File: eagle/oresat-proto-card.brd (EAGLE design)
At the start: 99.8 x 94.7 mm, 123 parts, among them J1 J-SAMTEC-TFM-110-X1-XXX-D-RA, J2 U.FL, J3 U.FL, J4 U.FL, J6 J-SAMTEC-TFM-120-X1-XXX-D-RA, J7 FTSH-105-XX-X-DV-K, Q1 DMP2240UDM, Q2 DMP2240UDM, Q3 MOSFET-PCH-SOT23-6, Q4 MOSFET-PCH-SOT23-6, Q5 PMV45EN, Q6 PMV45EN, U2 TCAN330, U3 MAX7310ATE, U4 MAX4211CETE, U5 TPS62111RSA, U6 STM32F042K6, X1 16MHZ-2.5x2mm

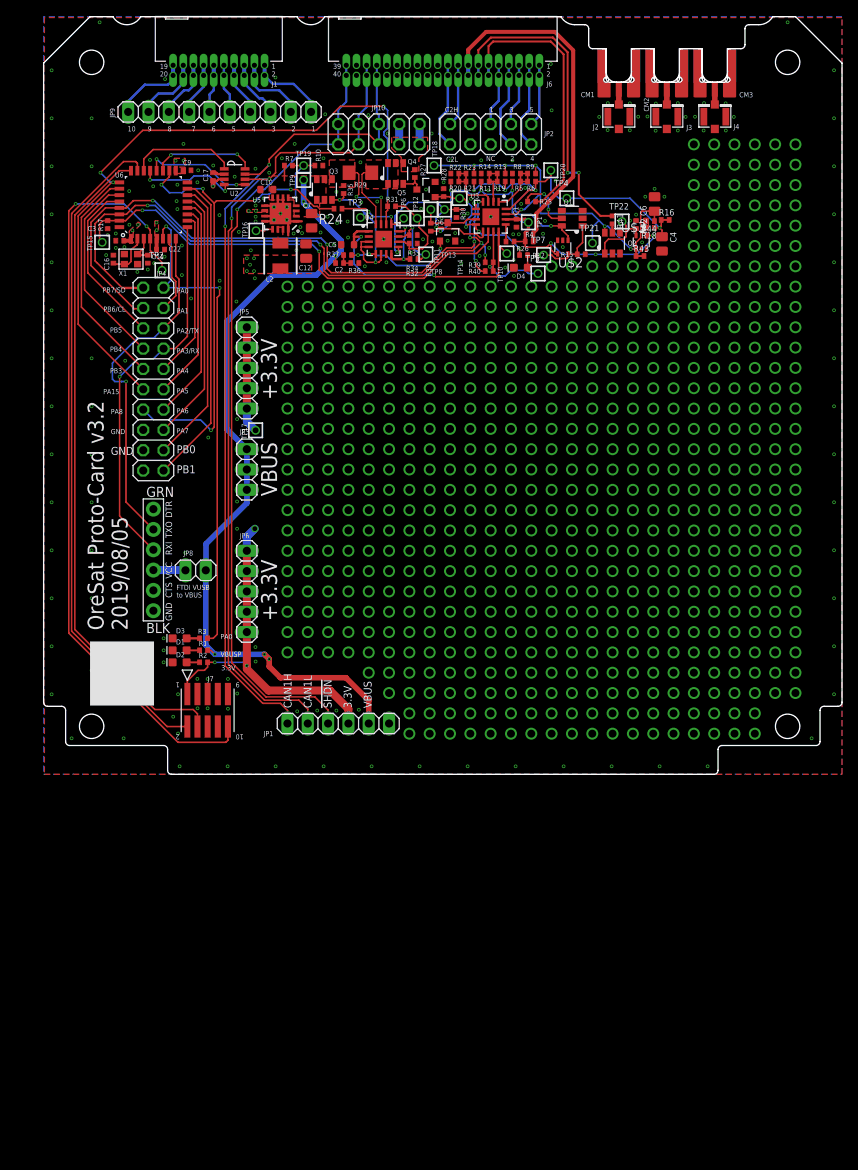
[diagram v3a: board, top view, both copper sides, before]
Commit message: fixed j-tag connect, final tweaks for 3.3, updated bom
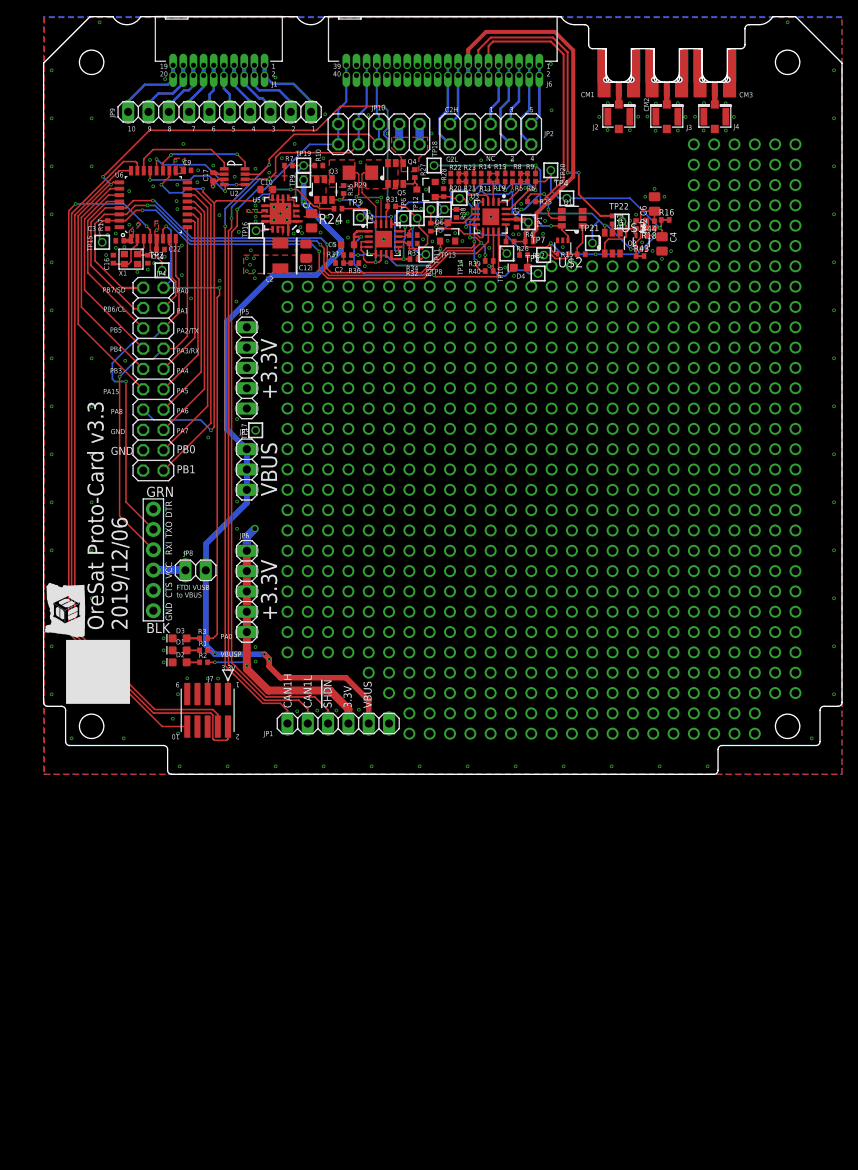
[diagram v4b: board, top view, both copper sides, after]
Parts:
- C4, C6, R16, R18, R43, R44: value NP -> TBD
- R42: value 10k -> TBD
- moved R39 0.17 mm to (55.7, 64.2)
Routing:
- net 3.3V: track 63.1 -> 46.2 mm, vias 17 -> 18
- net SWDIO: track 83.5 -> 92.8 mm
- net NRESET: track 97.7 -> 90.0 mm
- net SWCLK: track 82.4 -> 84.9 mm
- net IOUT: track 88.3 -> 87.5 mm
- net GND: vias 307 -> 306
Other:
- board text added: "2019/12/06"
- board text added: "OreSat Proto-Card v3.3"
- board text removed: "2019/08/05"
- board text removed: "OreSat Proto-Card v3.2"

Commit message: Now v3.3. New OPD I2C protection circuits. Move to 4 layers. Lots of cleanup and massaging, but nothing worth saying. Added ground ring around 3.3V ring on L15. Attributes are still wrong, needs to be cleaned up to make automatic BOM.
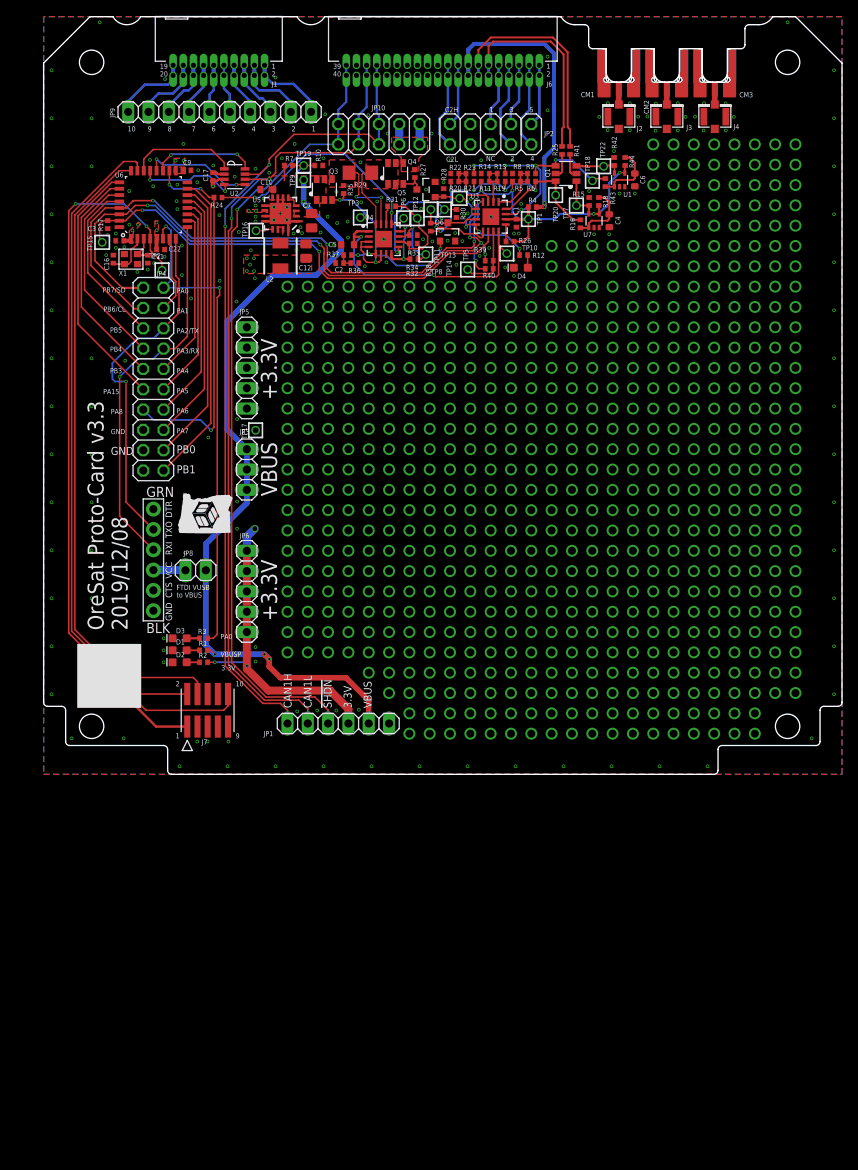
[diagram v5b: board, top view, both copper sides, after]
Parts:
- removed Q2: DMP2240UDM, Q-MOSFET-PCH-dual-SOT23-6:SOT23-6
- removed TP21, TP4: TEST-POINT, Tova:2MM-TEST-POINT
- removed U$2, U$3: MIC842, Q-Microchip-MIC842-Comparator:SC70-5
- added U1, U7: MIC842LYC5, Q-Microchip-MIC842-Comparator:SC70-5
- C4, C6: value TBD -> 1u; device oresat-rcl:.0805-B-NOSILK -> oresat-rcl:.0603-B-NOSILK
- R16, R43: value TBD -> 330k
- R18, R44: value TBD -> 1M
- R42: value TBD -> 10k
- U4: value MAX4211CETE -> MAX4211FETE
- moved TP18 19.9 mm to (68.6, 74.2)
- moved R24 15.1 mm to (21.8, 72.1)
- moved R16 10.6 mm to (67.1, 68.8), turned to 90 degrees
- moved R41 10.2 mm to (65.8, 78.0)
- moved R43 10.1 mm to (70.2, 74.0), turned to 90 degrees
- moved TP5 8.81 mm to (53.0, 63.1)
- moved R42 8.36 mm to (71.3, 76.6)
- moved R44 8.09 mm to (72.7, 76.6), turned to 270 degrees
- moved R25 7.44 mm to (64.8, 78.0), turned to 270 degrees
- moved TP7 7.43 mm to (66.6, 71.1)
- moved TP22 7.27 mm to (70.0, 76.0)
- moved R18 7.23 mm to (69.4, 71.6), turned to 270 degrees
- moved C4 7.21 mm to (70.7, 69.2)
- moved R15 6.68 mm to (68.2, 71.6), turned to 270 degrees
- moved Q1 5.65 mm to (65.3, 75.1)
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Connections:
- new net N$400: C6.1, R43.1, R44.1, U1.1
- new net N$401: C4.1, R16.1, R18.1, U7.1
- new net PA15: JP4.11, U6.25
- net GND: now also U1.2, U7.2; no longer U$2.2, U$3.2
- net IOUT: no longer JP4.11, U6.25
- net N$479: now also Q1.2; no longer Q2.5
- net N$480: now also Q1.3, U1.5; no longer Q2.1, U$3.5
- net N$580: now also U7.5; no longer U$2.5
- net PEN-SCL-FILT: now also Q1.4; no longer C6.1, Q2.6, R43.1, R44.1, TP21.1, U$3.1
- net PEN-SDA-FILT: no longer C4.1, R16.1, R18.1, TP4.1, U$2.1
- net VPD: now also U1.4, U7.4; no longer U$2.4, U$3.4
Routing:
- net IOUT: track 87.5 -> 2.31 mm, vias 4 -> 0
- net PA15: track 0.00 -> 32.0 mm
- net PEN-SDA-FILT: track 54.9 -> 26.2 mm, vias 5 -> 3
- net PEN-SCL-FILT: track 55.0 -> 30.5 mm, vias 6 -> 5
- net POUT: track 9.34 -> 30.6 mm
- net POUTPROT: track 65.2 -> 46.8 mm, vias 5 -> 3
- net OPD_SCL: track 40.2 -> 27.6 mm, vias 2 -> 0
- net SWDIO: track 92.8 -> 81.9 mm
- net OPD_SDA: track 34.3 -> 25.5 mm
- net OPD_PWR: track 44.2 -> 35.9 mm, vias 0 -> 2
- net N$401: track 0.00 -> 8.00 mm
- net N$400: track 0.00 -> 7.86 mm
- net 3.3V: track 46.2 -> 53.8 mm
- net NRESET: track 90.0 -> 95.9 mm
- net N$579: track 7.44 -> 3.08 mm, vias 2 -> 0
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- added copper zone on layer 15, net GND
- removed copper zone on layer 1, net VPD
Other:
- board text added: "2019/12/08"
- board text removed: "2019/12/06"

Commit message: fixing the lock?
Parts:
- J5: value (none) -> DNP

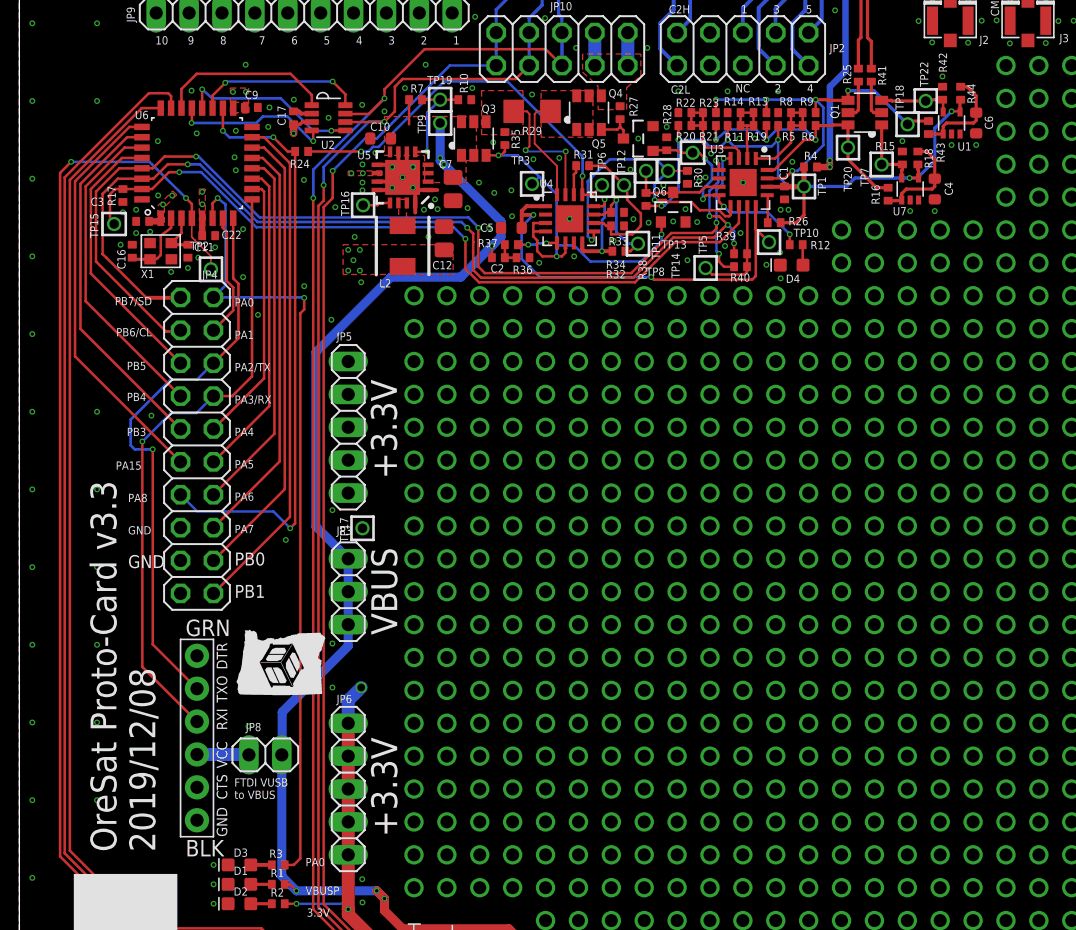
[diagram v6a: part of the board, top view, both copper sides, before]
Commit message: Fixed MIC842L flipped pins. Layout turned out to be better, too!
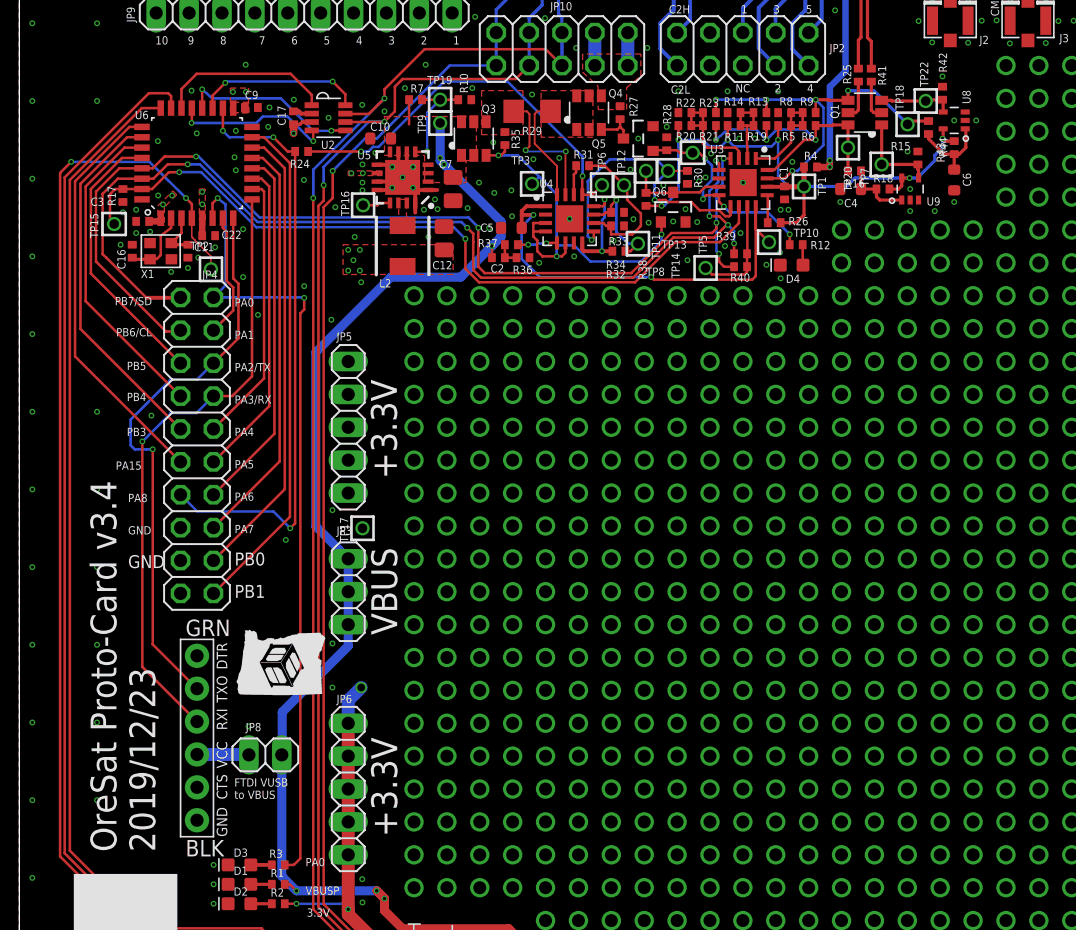
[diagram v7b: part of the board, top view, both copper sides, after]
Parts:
- removed U1, U7: MIC842LYC5, Q-Microchip-MIC842-Comparator:SC70-5
- added U8, U9: MIC842LYC5, U-Microchip-MIC842-Comparator:SC70-5
- moved C4 6.50 mm to (64.2, 69.2), turned to 180 degrees
- moved C6 4.72 mm to (72.2, 69.9)
- moved R44 4.23 mm to (72.2, 72.4), turned to 90 degrees
- moved R18 3.61 mm to (66.7, 69.2), turned to 0 degrees
- moved R16 3.16 mm to (64.5, 70.6), turned to 180 degrees
- moved R15 1.20 mm to (69.4, 71.6)
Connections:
- net GND: now also U8.2, U9.2; no longer U1.2, U7.2
- net N$400: now also U8.1; no longer U1.1
- net N$401: now also U9.1; no longer U7.1
- net N$480: now also U8.4; no longer U1.5
- net N$580: now also U9.4; no longer U7.5
- net VPD: now also U8.5, U9.5; no longer U1.4, U7.4
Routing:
- net PEN-SDA-FILT: track 26.2 -> 23.1 mm
- net N$401: track 8.00 -> 5.25 mm
- net VPD: track 51.7 -> 49.7 mm
- net N$400: track 7.86 -> 6.62 mm
- net N$580: track 5.72 -> 6.92 mm
- net GND: vias 295 -> 298
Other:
- board text added: "2019/12/23"
- board text added: "OreSat Proto-Card v3.4"
- board text removed: "2019/12/08"
- board text removed: "OreSat Proto-Card v3.3"

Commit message: protocard preliminary rev 3.5
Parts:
- removed C11, C16: 20p, rcl_custom:.0402-B-NOSILK
- removed C17, C22, C3, C9: 100n, rcl_custom:.0402-B-NOSILK
- removed D3: AMBER, SparkFun-LED:LED-0603
- removed J5: DNP, SparkFun-Connectors:6_PIN_SERIAL_TARGET_SIDE_W_SILK
- removed JP4: (no value), pinhead:2X10
- removed JP8: (no value), pinhead:1X02
- removed R17: 10k, rcl_custom:.0402-B-NOSILK
- removed R24: 10k, rcl:R0402
- removed R3: 2.7k, rcl_custom:.0402-B-NOSILK
- removed TP15, TP2: TEST-POINT, Tova:2MM-TEST-POINT
- removed U2: TCAN330, TCAN330:SOT23-8_TI-DCN
- removed U6: STM32F042K6, STM32F042K:QFP32-7X7
- removed X1: 16MHZ-2.5x2mm, low-gain-radio:CRYSTAL_2.5X2
- added C13, C14, C19, C20, C21: 100n, oresat-rcl:.0603-C-NOSILK
- added C15, C18: 20p, oresat-rcl:.0603-C-NOSILK
- added D5: AMBER, SparkFun-LED:LED-0603
- added JP7: (no value), pinhead:2X10
- added R47, R49: 10k, oresat-rcl:.0603-C-NOSILK
- added R48, R50, R51: 2.7k, oresat-rcl:.0603-C-NOSILK
- added TP26, TP27, TP28, TP29, TP30, TP31, TP32: TEST-POINT, Tova:2MM-TEST-POINT
- added U1: TCAN330, TCAN330:SOT23-8_TI-DCN
- added U7: STM32F091C, U-ST-STM32F091C-uC:STM32F091C
- added X2: 16MHZ-2.5x2mm, low-gain-radio:CRYSTAL_2.5X2
- J7: value FTSH-105-XX-X-DV-K -> ORESAT-DEBUG-CONNECTOR-CARD; device J-Samtec-FTSH-105-XXX-DV-K-ARM-SWD:CON10_2X5_DUK_FTSH -> oresat-edge_connector:TE_2-1734592-0
- R1, R2: device rcl_custom:.0402-B-NOSILK -> oresat-rcl:.0603-C-NOSILK
- moved JP1 31.2 mm to (18.2, 31.5), turned to 270 degrees
- moved J7 12.2 mm to (32.7, 7.90), turned to 180 degrees
- moved D2 0.30 mm to (17.0, 14.3)
- moved R2 0.30 mm to (20.0, 14.3)
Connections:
- removed net CRYSTALIN: C16.1, U6.2, X1.1
- removed net CRYSTALOUT: C11.1, U6.3, X1.3
- removed net N$1: D3.A, R3.1
- removed net N$406: J5.P$4, JP8.2
- new net CRYSTALIN1: C18.1, U7.5, X2.1
- new net CRYSTALOUT1: C15.1, U7.6, X2.3
- new net N$522: D5.A, R48.1
- new net N$523: J7.20, TP31.1
- new net N$524: J7.19, TP30.1
- new net N$525: J7.18, TP29.1
- new net N$526: J7.17, TP28.1
- new net N$527: J7.16, TP32.1
- new net VBAT: U7.1
- net 3.3V: now also C13.2, C14.2, C19.2, C20.2, C21.2, J7.11, R50.2, R51.2, U1.3, U7.24, U7.36, U7.48, U7.9; no longer C17.2, C22.2, C3.2, C9.2, J7.1, U2.3, U6.1, U6.17, U6.5
- net BOOT0: now also R47.2, TP26.1, U7.44; no longer R17.2, TP15.1, U6.31
- net CAN1_H: no longer U2.7
- net CAN1_L: no longer U2.6
- net CAN2_H: now also U1.7
- net CAN2_L: now also U1.6
- net CAN_RX: now also U1.4, U7.32; no longer U2.4, U6.21
- net CAN_SHDN: now also U1.5, U7.31; no longer U2.5, U6.20
- net CAN_SILENT: now also U1.8, U7.30; no longer U2.8, U6.19
- net CAN_TX: now also U1.1, U7.33; no longer U2.1, U6.22
- net GND: now also C13.1, C14.1, C15.2, C18.2, C19.1, C20.1, C21.1, D5.C, J7.6, J7.PAD1, J7.PAD2, JP7.15, JP7.17, JP7.19, R47.1, U1.2, U7.23, U7.35, U7.47, U7.8, X2.2, X2.4; no longer C11.2, C16.2, C17.1, C22.1, C3.1, C9.1, D3.C, J5.P$6, J7.5, JP4.15, JP4.17, JP4.19, R17.1, U2.2, U6.16, U6.32, X1.2, X1.4
- net NRESET: now also TP27.1, U7.7; no longer TP2.1, U6.4
- net PA0: now also JP7.2, R48.2, U7.10; no longer JP4.2, R3.2, U6.6
- net PA1: now also JP7.4, U7.11; no longer JP4.4, U6.7
- net PA15: now also JP7.11, U7.38; no longer JP4.11, U6.25
- net PA2/USART2_TX: now also J7.12, JP7.6, U7.12; no longer J5.P$2, JP4.6, U6.8
- net PA3/USART2_RX: now also J7.13, JP7.8, U7.13; no longer J5.P$3, JP4.8, U6.9
- net PA4: now also JP7.10, U7.14; no longer JP4.10, U6.10
- net PA5/SPI1_SCK: now also JP7.12, U7.15; no longer JP4.12, U6.11
- net PA6/SPI1_MISO: now also JP7.14, U7.16; no longer JP4.14, U6.12
- net PA7/SPI1_MOSI: now also JP7.16, U7.17; no longer JP4.16, U6.13
- net PB0: now also JP7.18, U7.18; no longer JP4.18, U6.14
- net PB1: now also JP7.20, U7.19; no longer JP4.20, U6.15
- net PB3: now also JP7.9, U7.39; no longer JP4.9, U6.26
- net PB4: now also JP7.7, U7.40; no longer JP4.7, U6.27
- net PB5: now also JP7.5, U7.41; no longer JP4.5, U6.28
- net PB6/SCL: now also JP7.3, R50.1, U7.42; no longer JP4.3, U6.29
- net PB7/SDA: now also JP7.1, R51.1, U7.43; no longer JP4.1, U6.30
- net POUT: now also R49.1; no longer R24.1
- net POUTPROT: now also JP7.13, R49.2, U7.29; no longer JP4.13, R24.2, U6.18
- net SWCLK: now also J7.15, U7.37; no longer J7.4, U6.24
- net SWDIO: now also J7.14, U7.34; no longer J7.2, U6.23
- net VBUS: now also J7.1, J7.2
- net VBUSP: no longer JP8.1
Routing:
- net VBUS: track 5.08 -> 80.6 mm, vias 0 -> 2
- net CAN2_L: track 10.9 -> 46.2 mm
- net CAN1_L: track 104.9 -> 70.0 mm
- net CAN1_H: track 106.4 -> 72.0 mm
- net CAN2_H: track 7.77 -> 41.0 mm
- net PA2/USART2_TX: track 44.1 -> 75.5 mm
- net !SD: track 99.4 -> 68.6 mm
- net 3.3V: track 53.8 -> 23.4 mm, vias 18 -> 20
- net PA3/USART2_RX: track 47.6 -> 76.8 mm
- net VBUSP: track 103.8 -> 81.1 mm, vias 6 -> 4
- net N$526: track 0.00 -> 13.8 mm
- net N$527: track 0.00 -> 13.1 mm
- net N$525: track 0.00 -> 9.65 mm
- net N$524: track 0.00 -> 7.09 mm
- net N$523: track 0.00 -> 6.97 mm
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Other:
- board text added: "OreSat Proto-Card v3.5"
- board text removed: "OreSat Proto-Card v3.4"
